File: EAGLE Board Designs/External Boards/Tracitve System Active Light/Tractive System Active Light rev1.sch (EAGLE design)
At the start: 25 parts, among them X1 CONNECTOR-4NANO-FIT-VERTICAL-4

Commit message: Later version of TSAL schematic and board
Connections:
- net N$12 renamed RED
- net N$7 renamed GRN
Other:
- moved on the sheet: C1, C2, C3, C4, C5, C6, LED1, LED2, LED3, LED4, LED5, LED6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

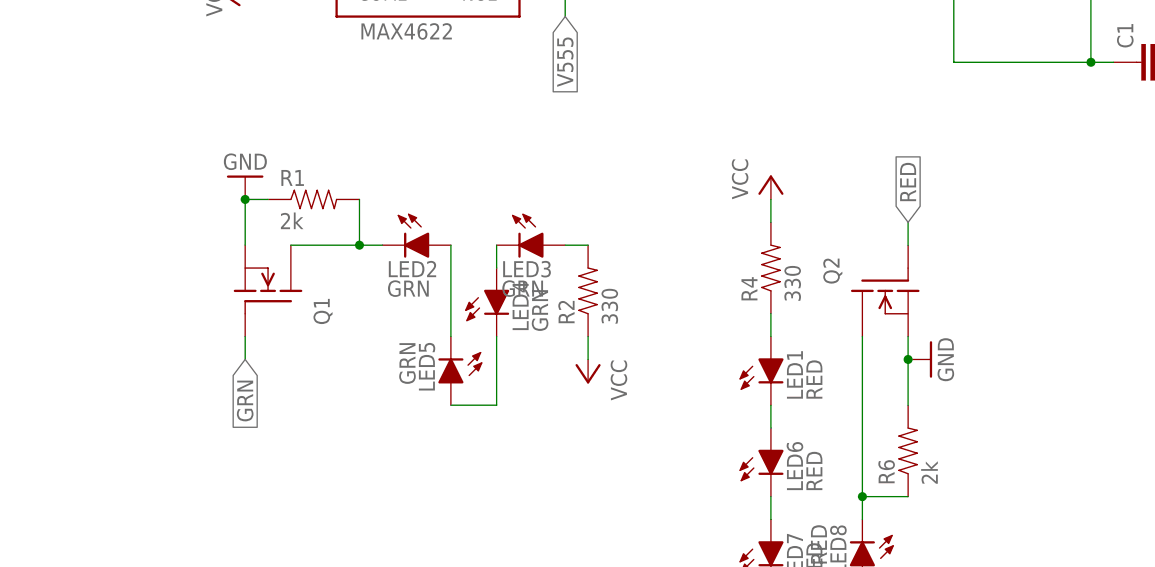
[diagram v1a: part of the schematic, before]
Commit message: Fixed pull-down transistors on gate
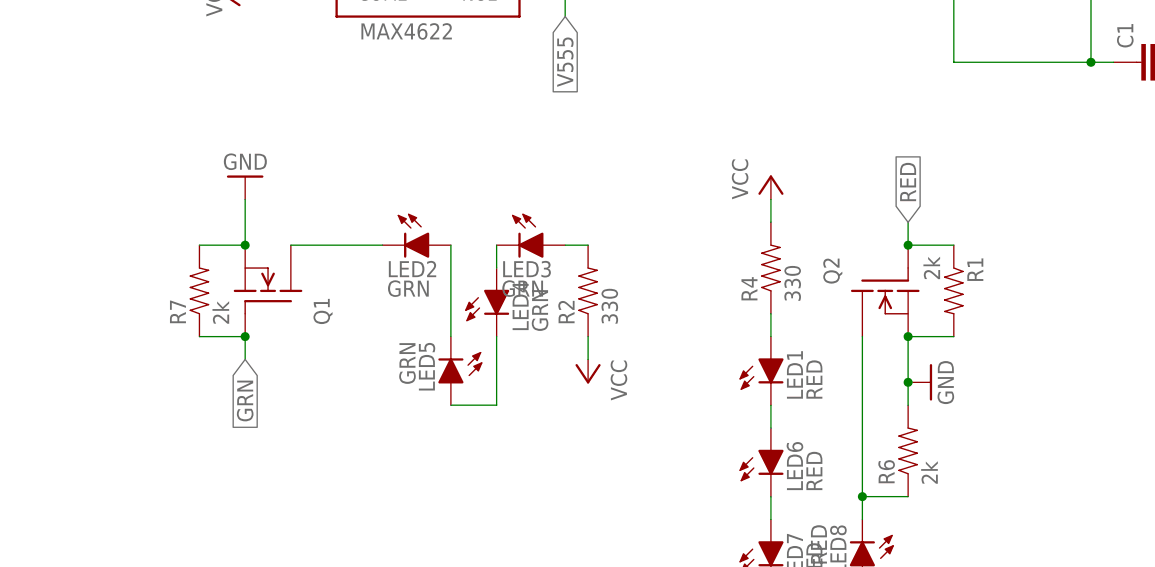
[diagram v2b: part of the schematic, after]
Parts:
- added R7: 2k, HyTechDevices:RESISTOR0603-RES
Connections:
- net GND: now also R1.2, R7.2; no longer R1.1
- net GRN: now also R7.1
- net N$2: no longer R1.2
- net RED: now also R1.1
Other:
- moved on the sheet: R1
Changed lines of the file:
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@@
 <?xml version="1.0" encoding="utf-8"?>
 <!DOCTYPE eagle SYSTEM "eagle.dtd">
-<eagle version="9.5.0">
+<eagle version="9.5.1">
 <drawing>
 <settings>
-<setting alwaysvectorfont="no"/>
+<setting alwaysvectorfont="yes"/>
 <setting verticaltext="up"/>
 </settings>
-<grid distance="0.1" unitdist="inch" unit="inch" style="lines" multiple="1" display="no" altdistance="0.01" altunitdist="inch" altunit="inch"/>
+<grid distance="0.1" unitdist="inch" unit="inch" style="lines" multiple="1" display="yes" altdistance="0.01" altunitdist="inch" altunit="inch"/>
 <layers>
 <layer number="1" name="Top" color="4" fill="1" visible="no" active="no"/>
@@
 <part name="LED1" library="HyTechDevices" deviceset="XP-E2" device="" value="RED"/>
 <part name="LED2" library="HyTechDevices" deviceset="XP-E2" device="" value="GRN"/>
-<part name="R1" library="HyTechDevices" deviceset="RESISTOR" device="0603-RES" value="2k"/>
 <part name="R3" library="HyTechDevices" deviceset="RESISTOR" device="0603-RES" value="50k"/>
 <part name="R4" library="HyTechDevices" deviceset="RESISTOR" device="0603-RES" value="330"/>
@@
 <part name="P+3" library="supply1" library_urn="urn:adsk.eagle:library:371" deviceset="VCC" device=""/>
 <part name="GND3" library="HyTechSymbols" deviceset="GND" device=""/>
+<part name="R7" library="HyTechDevices" deviceset="RESISTOR" device="0603-RES" value="2k"/>
+<part name="R1" library="HyTechDevices" deviceset="RESISTOR" device="0603-RES" value="2k"/>
 </parts>
 <sheets>
@@
 <attribute name="VALUE" x="-9.652" y="32.385" size="1.778" layer="96"/>
 </instance>
-<instance part="R1" gate="G$1" x="-17.78" y="43.18" smashed="yes">
-<attribute name="NAME" x="-21.59" y="44.6786" size="1.778" layer="95"/>
-<attribute name="VALUE" x="-21.59" y="39.878" size="1.778" layer="96"/>
-</instance>
 <instance part="R3" gate="G$1" x="53.34" y="81.28" smashed="yes" rot="R90">
 <attribute name="NAME" x="51.8414" y="77.47" size="1.778" layer="95" rot="R90"/>
@@
 <attribute name="VALUE" x="15.24" y="25.4" size="1.778" layer="96" rot="R270"/>
 </instance>
-<instance part="GND7" gate="1" x="50.8" y="25.4" smashed="yes" rot="R90">
-<attribute name="VALUE" x="53.34" y="22.86" size="1.778" layer="96" rot="R90"/>
+<instance part="GND7" gate="1" x="50.8" y="22.86" smashed="yes" rot="R90">
+<attribute name="VALUE" x="53.34" y="20.32" size="1.778" layer="96" rot="R90"/>
 </instance>
 <instance part="GND8" gate="1" x="17.78" y="78.74" smashed="yes" rot="R90">
@@
 <instance part="GND3" gate="1" x="22.86" y="109.22" smashed="yes" rot="R180">
 <attribute name="VALUE" x="25.4" y="111.76" size="1.778" layer="96" rot="R180"/>
+</instance>
+<instance part="R7" gate="G$1" x="-30.48" y="33.02" smashed="yes" rot="R90">
+<attribute name="NAME" x="-31.9786" y="29.21" size="1.778" layer="95" rot="R90"/>
+<attribute name="VALUE" x="-27.178" y="29.21" size="1.778" layer="96" rot="R90"/>
+</instance>
+<instance part="R1" gate="G$1" x="53.34" y="33.02" smashed="yes" rot="R270">
+<attribute name="NAME" x="54.8386" y="36.83" size="1.778" layer="95" rot="R270"/>
+<attribute name="VALUE" x="50.038" y="36.83" size="1.778" layer="96" rot="R270"/>
 </instance>
 </instances>
@@
 <pinref part="Q1" gate="G$1" pin="D"/>
 <pinref part="LED2" gate="&gt;NAME" pin="C"/>
-<wire x1="-20.32" y1="38.1" x2="-12.7" y2="38.1" width="0.1524" layer="91"/>
-<pinref part="R1" gate="G$1" pin="2"/>
-<wire x1="-12.7" y1="38.1" x2="-10.16" y2="38.1" width="0.1524" layer="91"/>
-<wire x1="-12.7" y1="43.18" x2="-12.7" y2="38.1" width="0.1524" layer="91"/>
-<junction x="-12.7" y="38.1"/>
+<wire x1="-20.32" y1="38.1" x2="-10.16" y2="38.1" width="0.1524" layer="91"/>
 </segment>
 </net>
@@
 </segment>
 <segment>
-<pinref part="R1" gate="G$1" pin="1"/>
-<wire x1="-22.86" y1="43.18" x2="-25.4" y2="43.18" width="0.1524" layer="91"/>
 <pinref part="Q1" gate="G$1" pin="S"/>
 <wire x1="-25.4" y1="38.1" x2="-25.4" y2="43.18" width="0.1524" layer="91"/>
 <pinref part="GND2" gate="1" pin="GND"/>
-<junction x="-25.4" y="43.18"/>
+<pinref part="R7" gate="G$1" pin="2"/>
+<wire x1="-30.48" y1="38.1" x2="-25.4" y2="38.1" width="0.1524" layer="91"/>
+<junction x="-25.4" y="38.1"/>
 </segment>
 <segment>
@@
 <segment>
 <pinref part="Q2" gate="G$1" pin="S"/>
-<wire x1="48.26" y1="20.32" x2="48.26" y2="25.4" width="0.1524" layer="91"/>
+<wire x1="48.26" y1="20.32" x2="48.26" y2="22.86" width="0.1524" layer="91"/>
 <pinref part="R6" gate="G$1" pin="2"/>
 <pinref part="GND7" gate="1" pin="GND"/>
-<wire x1="48.26" y1="25.4" x2="48.26" y2="27.94" width="0.1524" layer="91"/>
-<junction x="48.26" y="25.4"/>
+<wire x1="48.26" y1="22.86" x2="48.26" y2="27.94" width="0.1524" layer="91"/>
+<junction x="48.26" y="22.86"/>
+<pinref part="R1" gate="G$1" pin="2"/>
+<wire x1="53.34" y1="27.94" x2="48.26" y2="27.94" width="0.1524" layer="91"/>
+<junction x="48.26" y="27.94"/>
 </segment>
 <segment>
@@
 <wire x1="-25.4" y1="27.94" x2="-25.4" y2="25.4" width="0.1524" layer="91"/>
 <label x="-25.4" y="25.4" size="1.778" layer="95" rot="R270" xref="yes"/>
+<pinref part="R7" gate="G$1" pin="1"/>
+<wire x1="-30.48" y1="27.94" x2="-25.4" y2="27.94" width="0.1524" layer="91"/>
+<junction x="-25.4" y="27.94"/>
 </segment>
 </net>
@@
 <wire x1="48.26" y1="38.1" x2="48.26" y2="40.64" width="0.1524" layer="91"/>
 <label x="48.26" y="40.64" size="1.778" layer="95" rot="R90" xref="yes"/>
-</segment>
-</net>
+<pinref part="R1" gate="G$1" pin="1"/>
+<wire x1="53.34" y1="38.1" x2="48.26" y2="38.1" width="0.1524" layer="91"/>
+<junction x="48.26" y="38.1"/>
+</segment>
+</net>
